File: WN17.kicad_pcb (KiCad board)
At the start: 2 copper layers, 41 x 46 mm, 15 parts, among them J1 Conn_01x02_Pin, U1 AS5600, U2 DRV8434APWPR, U3 STM32L476RGTx, U4 ESP-12F, U5 AMS1117

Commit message: Updates
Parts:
- added C10: 10u, Capacitor_SMD:C_0603_1608Metric_Pad1.08x0.95mm_HandSolder, F.Cu at (117.5, 75.3)
- added C11: 10n, Capacitor_SMD:C_0603_1608Metric_Pad1.08x0.95mm_HandSolder, F.Cu at (117.5, 85.2)
- added C12: 1u, Capacitor_SMD:C_0603_1608Metric_Pad1.08x0.95mm_HandSolder, F.Cu at (117.5, 83.2)
- added C13: 1u, Capacitor_SMD:C_0603_1608Metric_Pad1.08x0.95mm_HandSolder, F.Cu at (124.2, 69.2)
- added C8: 10u, Capacitor_SMD:C_0603_1608Metric_Pad1.08x0.95mm_HandSolder, F.Cu at (133.9, 87.4)
- added C9: 10u, Capacitor_SMD:C_0603_1608Metric_Pad1.08x0.95mm_HandSolder, F.Cu at (134.4, 71.5)
- added FB1: 120R, Inductor_SMD:L_0603_1608Metric_Pad1.05x0.95mm_HandSolder, F.Cu at (117.6, 81.3)
- C7: value C_Polarized -> 22uF/50V
- moved U5 6.59 mm to (107.2, 78.0), turned to 0 degrees
- moved C7 6.47 mm to (98.5, 78.0)
- moved C5 1.10 mm to (125.2, 92.5)
- moved R1 0.98 mm to (124.3, 89.4), turned to 90 degrees
- moved C6 0.95 mm to (108.9, 88.7)
- moved C3 0.95 mm to (125.3, 94.5)
- moved C4 0.87 mm to (109.8, 91.6), turned to 90 degrees
- moved U4 0.70 mm to (113.0, 59.8)
- moved C2 0.66 mm to (108.8, 94.5)
- moved C1 0.47 mm to (104.1, 85.2)
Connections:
- Coils1 pad 1: unconnected-(Coils1-Pin_1-Pad1) -> DRV-BOUT1
- Coils1 pad 2: unconnected-(Coils1-Pin_2-Pad2) -> DRV-BOUT2
- Coils1 pad 3: unconnected-(Coils1-Pin_3-Pad3) -> DRV-AOUT2
- Coils1 pad 4: unconnected-(Coils1-Pin_4-Pad4) -> DRV-AOUT1
- J1 pad 1: Net-(J1-Pin_1) -> VDD
- U3 pad 1: unconnected-(U3-VBAT-Pad1) -> +3.3V
- U3 pad 12: unconnected-(U3-VSSA-Pad12) -> GND
- U3 pad 13: unconnected-(U3-VDDA-Pad13) -> +3.3VA
- U3 pad 18: Net-(U3-VSS-Pad18) -> GND
- U3 pad 19: unconnected-(U3-VDD-Pad19) -> +3.3V
- U3 pad 31: Net-(U3-VSS-Pad18) -> GND
- U3 pad 32: unconnected-(U3-VDD-Pad32) -> +3.3V
- U3 pad 47: Net-(U3-VSS-Pad18) -> GND
- U3 pad 48: unconnected-(U3-VDDUSB-Pad48) -> +3.3V
- U3 pad 63: Net-(U3-VSS-Pad18) -> GND
- U3 pad 64: unconnected-(U3-VDD-Pad64) -> +3.3V
- U4 pad 1: unconnected-(U4-~{RST}-Pad1) -> ESP_RST
- U4 pad 15: unconnected-(U4-GND-Pad15) -> GND
- U4 pad 21: unconnected-(U4-GPIO3/RXD-Pad21) -> ESP_RXD
- U4 pad 22: unconnected-(U4-GPIO1/TXD-Pad22) -> ESP_TXD
- U4 pad 3: unconnected-(U4-EN-Pad3) -> ESP_EN
- U4 pad 8: unconnected-(U4-VCC-Pad8) -> +3.3V
- U5 pad 3: Net-(J1-Pin_1) -> VDD

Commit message: Clock
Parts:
- added C14: 10u, Capacitor_SMD:C_0603_1608Metric_Pad1.08x0.95mm_HandSolder, F.Cu at (129.3, 69.6)
- added C15: 10u, Capacitor_SMD:C_0603_1608Metric_Pad1.08x0.95mm_HandSolder, F.Cu at (113.3, 78.3)
- added C16: 10u, Capacitor_SMD:C_0603_1608Metric_Pad1.08x0.95mm_HandSolder, F.Cu at (114.2, 75.2)
- added R2: 10k, Resistor_SMD:R_0603_1608Metric_Pad0.98x0.95mm_HandSolder, F.Cu at (127.1, 69.6)
- added Y1: 16MHz, Crystal:Crystal_SMD_3225-4Pin_3.2x2.5mm_HandSoldering, F.Cu at (117.5, 79.0)
- moved C1 6.17 mm to (107.5, 90.3)
- moved U5 5.52 mm to (104.8, 83.0)
- moved FB1 5.22 mm to (113.2, 84.1)
- moved C6 5.01 mm to (113.2, 86.0)
- moved C9 3.54 mm to (131.4, 69.6)
- moved C10 1.12 mm to (118.6, 75.2)
- moved C8 0.91 mm to (134.3, 86.6)
- moved C12 0.90 mm to (117.5, 84.1)
- moved C11 0.85 mm to (117.5, 86.0)
- moved C13 0.84 mm to (125.0, 69.6)
- moved C7 0.39 mm to (98.3, 78.2)
- moved C4 0.35 mm to (110.2, 91.6)
- moved C2 0.35 mm to (109.2, 94.5)
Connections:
- U3 pad 5: unconnected-(U3-PH0-Pad5) -> CLK_IN
- U3 pad 6: unconnected-(U3-PH1-Pad6) -> CLK_OUT
- U3 pad 60: unconnected-(U3-BOOT0-Pad60) -> Net-(U3-BOOT0)
- U3 pad 7: unconnected-(U3-NRST-Pad7) -> Net-(U3-NRST)

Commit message: uPDATE
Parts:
- added J2: SWD, Connector_PinHeader_1.00mm:PinHeader_1x03_P1.00mm_Vertical, F.Cu at (133.0, 94.8)
- added R3: 0.01R, Resistor_SMD:R_1206_3216Metric_Pad1.30x1.75mm_HandSolder, F.Cu at (105.4, 84.4)
- added U6: MCP6C02T-020E/CHY, mcp6c02:SOT-23-6_CHY_MCH, F.Cu at (101.9, 84.7)
- J1: value Conn_01x02_Pin -> PowerIn
- moved U5 5.83 mm to (106.7, 77.4)
- moved C9 2.15 mm to (133.6, 69.7)
- moved C7 0.81 mm to (98.5, 77.5)
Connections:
- J1 pad 1: VDD -> Net-(J1-Pin_1)
- U3 pad 3: unconnected-(U3-PC14-Pad3) -> ESP_EN
- U3 pad 4: unconnected-(U3-PC15-Pad4) -> ESP_RST
- U3 pad 46: unconnected-(U3-PA13-Pad46) -> SWDIO
- U3 pad 49: unconnected-(U3-PA14-Pad49) -> SWDCLK
- U3 pad 51: unconnected-(U3-PC10-Pad51) -> ESP_RXD
- U3 pad 52: unconnected-(U3-PC11-Pad52) -> ESP_TXD
- U4 pad 18: unconnected-(U4-GPIO0-Pad18) -> GND

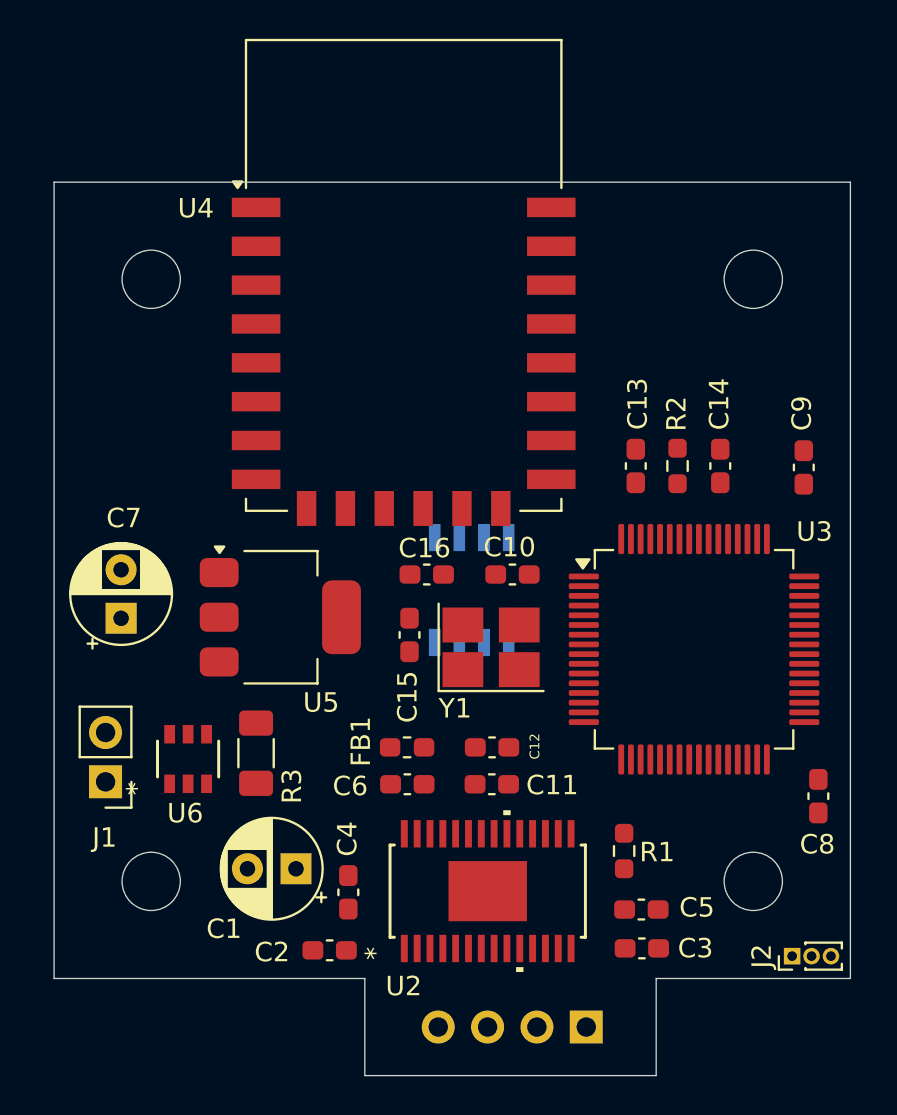
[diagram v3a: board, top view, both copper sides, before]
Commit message: Schematic done
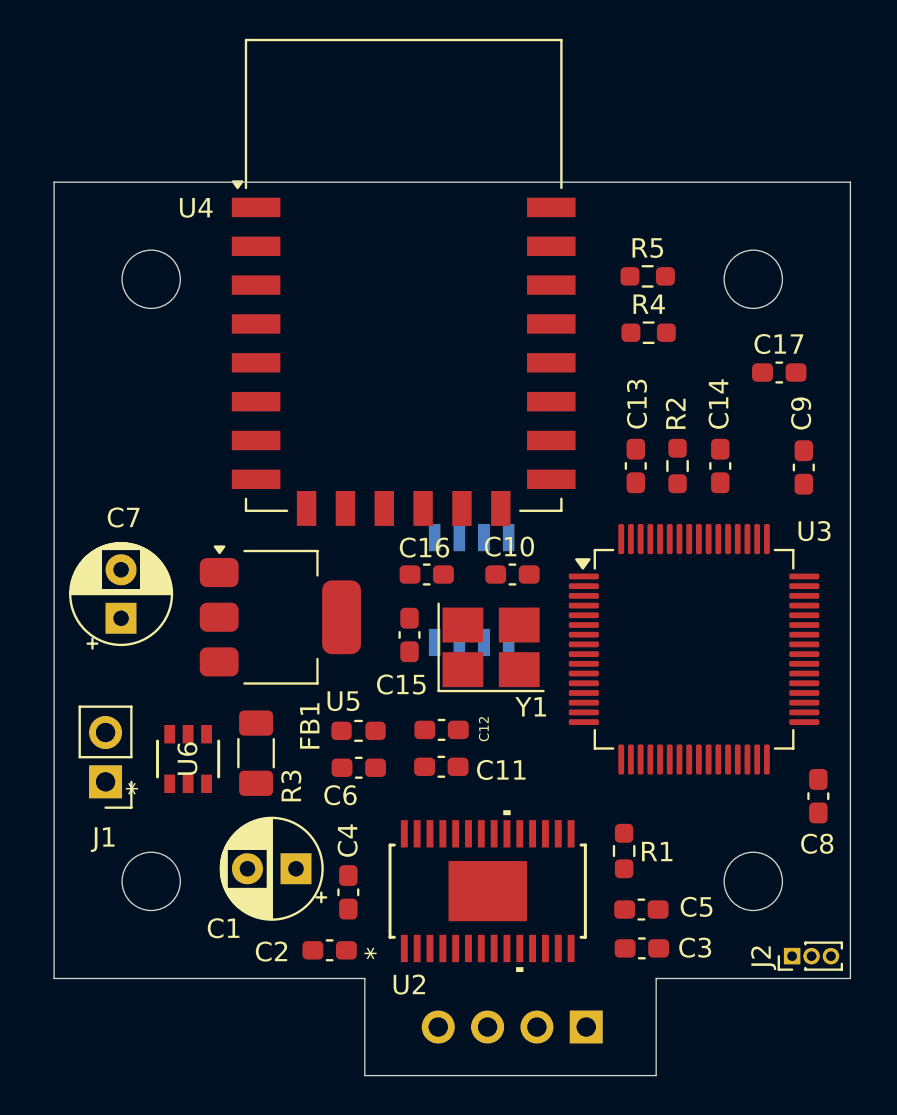
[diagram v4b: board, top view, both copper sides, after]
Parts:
- added C17: 100nF, Capacitor_SMD:C_0603_1608Metric_Pad1.08x0.95mm_HandSolder, F.Cu at (132.3, 64.8)
- added R4: 10k, Resistor_SMD:R_0603_1608Metric_Pad0.98x0.95mm_HandSolder, F.Cu at (125.6, 62.8)
- added R5: 10k, Resistor_SMD:R_0603_1608Metric_Pad0.98x0.95mm_HandSolder, F.Cu at (125.6, 59.9)
- moved C11 2.75 mm to (114.9, 85.1)
- moved C12 2.75 mm to (115.0, 83.2)
- moved C6 2.64 mm to (110.7, 85.2)
- moved FB1 2.64 mm to (110.7, 83.2)
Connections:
- U1 pad 1: unconnected-(U1-VDD5V-Pad1) -> +3.3V
- U1 pad 2: unconnected-(U1-VDD3V3-Pad2) -> +3.3V
- U1 pad 3: unconnected-(U1-OUT-Pad3) -> AS5600_OUT
- U1 pad 4: unconnected-(U1-GND-Pad4) -> GND
- U1 pad 5: unconnected-(U1-PGO-Pad5) -> AS5600_PGO
- U1 pad 6: unconnected-(U1-SDA-Pad6) -> AS5600_SDA
- U1 pad 7: unconnected-(U1-SCL-Pad7) -> AS5600_SCL
- U1 pad 8: unconnected-(U1-DIR-Pad8) -> AS5600_DIR
- U3 pad 10: unconnected-(U3-PC2-Pad10) -> DRV-M0
- U3 pad 11: unconnected-(U3-PC3-Pad11) -> DRV-M1
- U3 pad 14: unconnected-(U3-PA0-Pad14) -> MCP6C02_VOUT
- U3 pad 15: unconnected-(U3-PA1-Pad15) -> AS5600_OUT
- U3 pad 20: unconnected-(U3-PA4-Pad20) -> DRV-VREF
- U3 pad 25: unconnected-(U3-PC5-Pad25) -> nFault
- U3 pad 37: unconnected-(U3-PC6-Pad37) -> DRV-ENABLE
- U3 pad 38: unconnected-(U3-PC7-Pad38) -> DRV-NSLEEP
- U3 pad 39: unconnected-(U3-PC8-Pad39) -> DRV-DIR
- U3 pad 40: unconnected-(U3-PC9-Pad40) -> DRV-STEP
- U3 pad 58: unconnected-(U3-PB6-Pad58) -> AS5600_PGO
- U3 pad 59: unconnected-(U3-PB7-Pad59) -> AS5600_DIR
- U3 pad 61: unconnected-(U3-PB8-Pad61) -> AS5600_SCL
- U3 pad 62: unconnected-(U3-PB9-Pad62) -> AS5600_SDA
